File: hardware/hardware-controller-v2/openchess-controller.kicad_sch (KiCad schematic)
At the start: 30 parts, among them J1 Conn_02x13, J3 J_PANEL XH-10, M1 Lipo Rider Plus, U2 ESP32-DevKitC, U3 74AHCT125, U6 TBD62783A

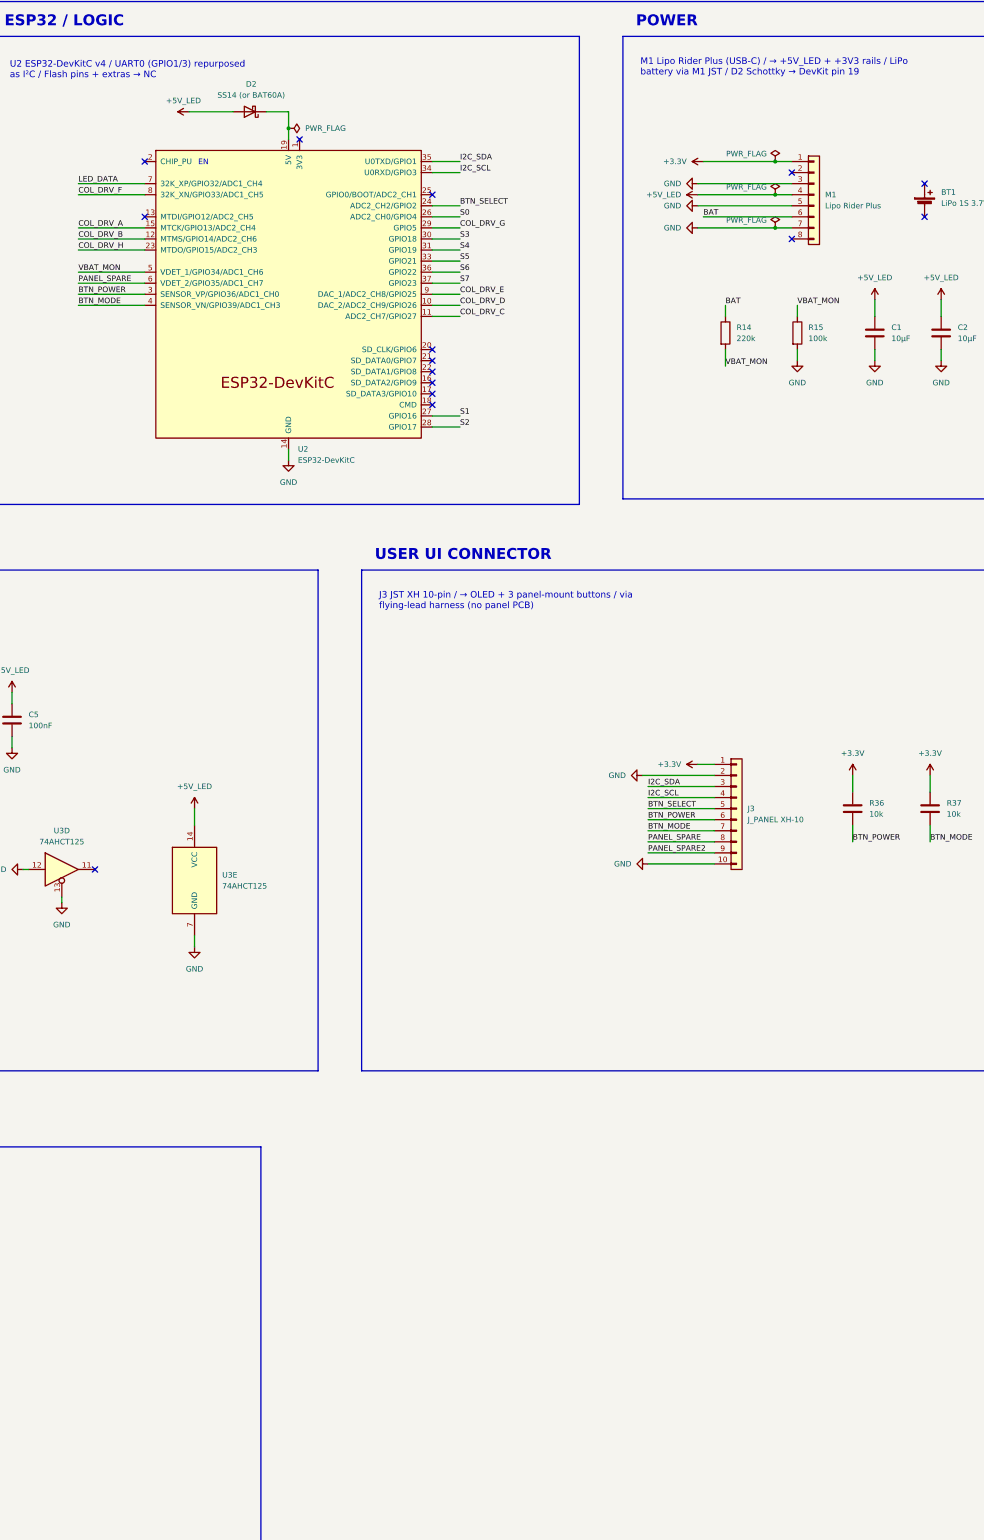
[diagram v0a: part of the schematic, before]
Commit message: feat(hw): v2 sch — WROOM-32E core hand-wired (power, EN/BOOT circuit)
Co-Authored-By: Claude Fable 5 <noreply@anthropic.com>
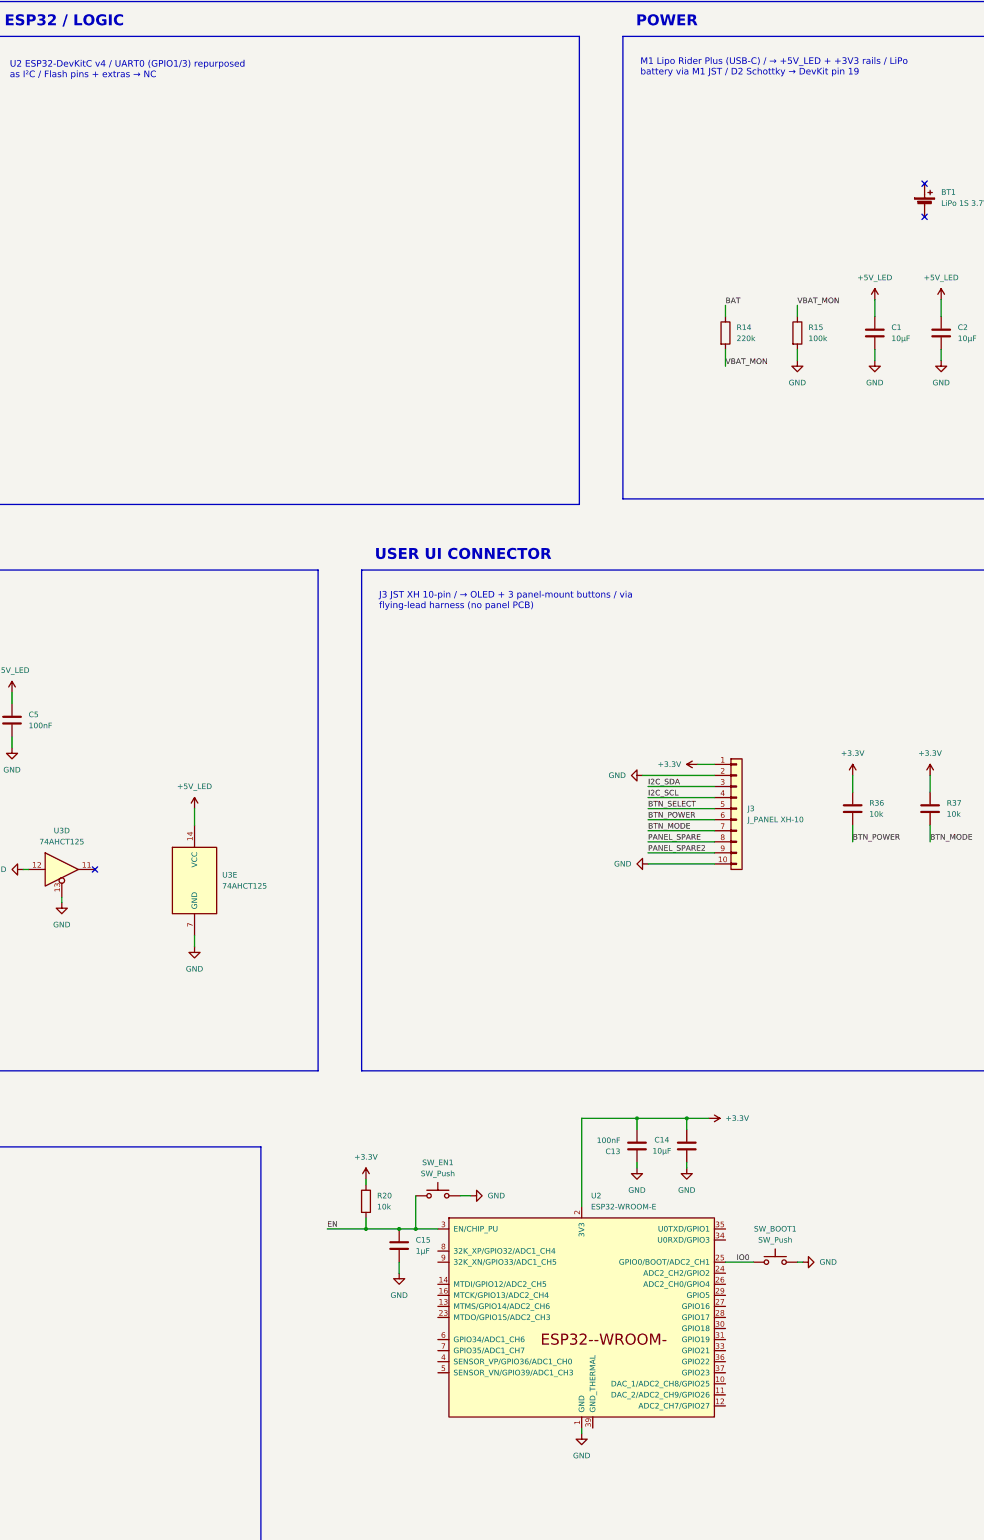
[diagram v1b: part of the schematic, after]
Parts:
- removed D2: SS14 (or BAT60A), Diode_SMD:D_SMA, symbol Device:D_Schottky
- removed M1: Lipo Rider Plus, Connector_PinSocket_2.54mm:PinSocket_1x08_P2.54mm_Vertical, symbol Connector_Generic:Conn_01x08
- removed U2: ESP32-DevKitC, Espressif:ESP32-DevKitC, symbol Espressif_Official:ESP32-DevKitC
- added C13: 100nF, symbol Device:C
- added C14: 10µF, symbol Device:C
- added C15: 1µF, symbol Device:C
- added R20: 10k, symbol Device:R
- added SW_BOOT1, SW_EN1: SW_Push, symbol Switch:SW_Push
- added U2: ESP32-WROOM-E, PCM_Espressif:ESP32-WROOM-32E, symbol Espressif_Official:ESP32-WROOM-E
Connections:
- net +3.3V: now also C13.1, C14.2, R20.1, U2.2 (3V3)
- net GND: now also C13.2, C14.1, C15.2, SW_BOOT1.2, SW_EN1.2, U2.1 (GND), U2.15 (GND), U2.38 (GND)
- new net EN: C15.1, R20.2, SW_EN1.1, U2.3 (EN/CHIP_PU)
- new net IO0: SW_BOOT1.1, U2.25 (GPIO0/BOOT/ADC2_CH1)
- no-connect marks 17 -> 5
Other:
- note removed: "EN"

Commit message: feat(hw): v2 sch — all 26 GPIO signal labels on WROOM core (27/27 contract)
Co-Authored-By: Claude Fable 5 <noreply@anthropic.com>
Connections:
- net BTN_MODE: now also U2.5 (SENSOR_VN/GPIO39/ADC1_CH3)
- net BTN_POWER: now also U2.4 (SENSOR_VP/GPIO36/ADC1_CH0)
- net BTN_SELECT: now also U2.24 (ADC2_CH2/GPIO2)
- net COL_DRV_A: now also U2.16 (MTCK/GPIO13/ADC2_CH4)
- net COL_DRV_B: now also U2.13 (MTMS/GPIO14/ADC2_CH6)
- net COL_DRV_C: now also U2.12 (ADC2_CH7/GPIO27)
- net COL_DRV_D: now also U2.11 (DAC_2/ADC2_CH9/GPIO26)
- net COL_DRV_E: now also U2.10 (DAC_1/ADC2_CH8/GPIO25)
- net COL_DRV_F: now also U2.9 (32K_XN/GPIO33/ADC1_CH5)
- net COL_DRV_G: now also U2.26 (ADC2_CH0/GPIO4)
- net COL_DRV_H: now also U2.14 (MTDI/GPIO12/ADC2_CH5)
- net GND: now also U2.39 (GND_THERMAL)
- net I2C_SCL: now also U2.36 (GPIO22)
- net I2C_SDA: now also U2.33 (GPIO21)
- net LED_DATA: now also U2.8 (32K_XP/GPIO32/ADC1_CH4)
- net S0: now also U2.27 (GPIO16)
- net S1: now also U2.28 (GPIO17)
- net S2: now also U2.30 (GPIO18)
- net S3: now also U2.31 (GPIO19)
- net S4: now also U2.37 (GPIO23)
- net S5: now also U2.29 (GPIO5)
- net S6: now also U2.23 (MTDO/GPIO15/ADC2_CH3)
- net S7: now also U2.7 (GPIO35/ADC1_CH7)
- net VBAT_MON: now also U2.6 (GPIO34/ADC1_CH6)
- net U0RXD: now reaches U2.34 (U0RXD/GPIO3)
- net U0TXD: now reaches U2.35 (U0TXD/GPIO1)
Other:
- note added: "OpenChess — Controller Board V2"
- note removed: "OpenChess — Controller Board"
- moved on the sheet: C15, R20, SW_BOOT1

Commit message: feat(hw): v2 sch — USB-C, CH340C, auto-program, ESD hand-wired (45/45 contract)
Co-Authored-By: Claude Fable 5 <noreply@anthropic.com>
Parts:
- added C16, C19: 100nF, symbol Device:C
- added J4: TYPE-C-31-M-12, symbol Connector:USB_C_Receptacle_USB2.0_16P
- added Q1, Q2: S8050 J3Y, Package_TO_SOT_SMD:SOT-23, symbol Transistor_BJT:SS8050
- added R21, R22: 5.1k, symbol Device:R
- added R23, R24: 10k, symbol Device:R
- added U7: CH340C, Package_SO:SOIC-16_3.9x9.9mm_P1.27mm, symbol Interface_USB:CH340C
- added U8: USBLC6-2SC6, Package_TO_SOT_SMD:SOT-23-6, symbol Power_Protection:USBLC6-2SC6
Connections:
- net EN: now also Q1.3 (C)
- net GND: now also C16.2, C19.2, J4.A1 (GND), J4.A12 (GND), J4.B1 (GND), J4.B12 (GND), J4.SH (SHIELD), R21.2, R22.2, U7.1 (GND), U8.2 (GND)
- net IO0: now also Q2.3 (C)
- net U0RXD: now also U7.2 (TXD)
- net U0TXD: now also U7.3 (RXD)
- new net: J4.A5 (CC1), R21.1
- new net: Q2.1 (B), R24.2
- new net: C19.1, U7.4 (V3)
- new net: J4.B5 (CC2), R22.1
- new net: Q1.1 (B), R23.2
- new net DTR: Q2.2 (E), R23.1, U7.13 (~{DTR})
- new net RTS: Q1.2 (E), R24.1, U7.14 (~{RTS})
- new net USB_DM: J4.A7 (D-), J4.B7 (D-), U7.6 (UD-), U8.3 (I/O2), U8.4 (I/O2)
- new net USB_DP: J4.A6 (D+), J4.B6 (D+), U7.5 (UD+), U8.1 (I/O1), U8.6 (I/O1)
- new net VBUS: C16.1, J4.A4 (VBUS), J4.A9 (VBUS), J4.B4 (VBUS), J4.B9 (VBUS), U7.16 (VCC), U8.5 (VBUS)
- no-connect marks 5 -> 12
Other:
- moved on the sheet: C13, C14, C15, R20, SW_BOOT1, SW_EN1, U2

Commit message: feat(hw): v2 sch — power chain hand-wired (80/80); checker refs adjudicated to as-built
R28/R29 and C17/C18 reference names landed swapped vs the guide; values sit on
the correct nets (1.1k=ILIM, 910R=ISET, 10uF on both LDO rails). As-built names
accepted; checker updated to match.

Co-Authored-By: Claude Fable 5 <noreply@anthropic.com>
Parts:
- removed BT1: LiPo 1S 3.7V (protected), symbol Device:Battery_Cell
- added C17, C18, C20, C21, C22: 10µF, symbol Device:C
- added C23: 100µF, symbol Device:C
- added C24, C25: 22µF, symbol Device:C
- added D4, D5: D, symbol Device:D
- added J5: B2B-XH-A, symbol Connector_Generic:Conn_01x02
- added L1: 1µH, symbol Device:L
- added R25, R27: 1k, symbol Device:R
- added R26: 100k, symbol Device:R
- added R28: 1.1K, symbol Device:R
- added R29: 910Ω, symbol Device:R
- added R30, R31, R32: 10k, symbol Device:R
- added SW1: MSK12C02, symbol Switch:SW_SPDT
- added U10: TPS61022RWUR, Package_DFN_QFN:Texas_RWU0007A_VQFN-7_2x2mm_P0.5mm, symbol Converter_DCDC:TPS61022
- added U11: AMS1117-3.3, Package_TO_SOT_SMD:SOT-223-3_TabPin2, symbol Regulator_Linear:AMS1117-3.3
- added U9: BQ24074RGTR, Package_DFN_QFN:VQFN-16-1EP_3x3mm_P0.5mm_EP1.6x1.6mm, symbol Battery_Management:BQ24074RGT
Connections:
- net +3.3V: now also C17.1, R27.1, U11.2 (VO), U9.5 (EN2)
- net +5V_LED: now also C18.1, C23.1, C24.1, C25.1, L1.2, R31.1, U10.3 (VOUT), U11.3 (VI)
- net GND: now also C17.2, C18.2, C20.1, C21.1, C22.1, C23.2, C24.2, C25.2, D5.1 (K), J5.2 (Pin_2), R26.2, R28.1, R29.1, R30.2, R32.2, U10.1 (GND), U10.6 (MODE), U11.1 (GND), U9.14 (TMR), U9.17 (VSS), U9.4 (~{CE}), U9.6 (EN1), U9.8 (VSS)
- net VBUS: now also C20.2, U9.13 (IN)
- net BAT renamed VBAT
- net VBAT: now also J5.1 (Pin_1), U9.2 (BAT), U9.3 (BAT)
- new net: L1.1, U10.2 (SW)
- new net: R31.2, R32.1, U10.4 (FB)
- new net: R26.1, SW1.1 (A), U10.5 (EN)
- new net: D5.2 (A), R27.2
- new net: R30.1, U9.1 (TS)
- new net: R28.2, U9.12 (ILIM)
- new net: R29.2, U9.16 (ISET)
- new net: D4.1 (K), U9.9 (~{CHG})
- new net: D4.2 (A), R25.1
- new net VSYS: C21.2, C22.2, R25.2, SW1.2 (B), U10.7 (VIN), U9.10 (OUT), U9.11 (OUT)
- no-connect marks 12 -> 13
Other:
- note added: "M1 Lipo Rider Plus (USB-C) / → +5V_LED + +3V3 rails / LiPo battery via M1 JST → DevKit pin 19"
- note removed: "M1 Lipo Rider Plus (USB-C) / → +5V_LED + +3V3 rails / LiPo battery via M1 JST / D2 Schottky → DevKit pin 19"
- moved on the sheet: C1, C11, C12, C13, C14, C15, C16, C19, C2, C5, FID1, FID2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

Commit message: fix(hw): v2 sch — FB divider values 750k/100k; checker now asserts component values
R31/R32 were both 10k (boost would regulate to 1.2V, not 5V) — caught by Paolo
visually; checker gap closed with value assertions for all power components.

Co-Authored-By: Claude Fable 5 <noreply@anthropic.com>
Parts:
- R31: value 10k -> 750k
- R32: value 10k -> 100k
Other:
- note removed: "M1 Lipo Rider Plus (USB-C) / → +5V_LED + +3V3 rails / LiPo battery via M1 JST → DevKit pin 19"
- note removed: "POWER"
- moved on the sheet: C1, C12, C16, C19, C2, FID1, FID2, FID3, FID4, J3, J4, Q1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

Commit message: feat(hw): v2 sch — panel split J6 OLED + J7/J8/J9 per-button XH-2; nets renamed BTN_UP/DOWN/OK
Button semantics follow firmware reality (ui_oled.cpp: UP/DOWN/OK; OK doubles
as deep-sleep wake). No dedicated power button; SW1 slide is power.

Co-Authored-By: Claude Fable 5 <noreply@anthropic.com>
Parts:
- removed J3: J_PANEL XH-10, Connector_PinHeader_2.54mm:PinHeader_1x10_P2.54mm_Vertical, symbol Connector_Generic:Conn_01x10
- added J6: J_OLED XH-4, symbol Connector_Generic:Conn_01x04
- added J7: J_BTN_UP XH-2, symbol Connector_Generic:Conn_01x02
- added J8: J_BTN_DOWN XH-2, symbol Connector_Generic:Conn_01x02
- added J9: J_BTN_OK XH-2, symbol Connector_Generic:Conn_01x02
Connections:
- net +3.3V: now also J6.2 (Pin_2)
- net GND: now also J6.1 (Pin_1), J7.2 (Pin_2), J8.2 (Pin_2), J9.2 (Pin_2)
- net I2C_SCL: now also J6.3 (Pin_3)
- net I2C_SDA: now also J6.4 (Pin_4)
- net BTN_MODE renamed BTN_DOWN
- net BTN_DOWN: now also J8.1 (Pin_1)
- net BTN_POWER renamed BTN_UP
- net BTN_UP: now also J7.1 (Pin_1)
- net BTN_SELECT renamed BTN_OK
- net BTN_OK: now also J9.1 (Pin_1)

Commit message: feat(hw): v2 sch — ERC zero errors (PWR_FLAG on GND); schematic wiring complete
Co-Authored-By: Claude Fable 5 <noreply@anthropic.com>
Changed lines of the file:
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@@
 	)
 	(junction
-		(at 354.33 273.0032)
+		(at 469.9 289.56)
 		(diameter 0)
 		(color 0 0 0 0)
 	)
 	(junction
-		(at 469.9 289.56)
+		(at 354.33 273.05)
 		(diameter 0)
 		(color 0 0 0 0)
@@
 	)
 	(junction
+		(at 360.68 147.32)
+		(diameter 0)
+		(color 0 0 0 0)
+	)
+	(junction
 		(at 457.2 303.53)
 		(diameter 0)
@@
 	(wire
 		(pts
-			(xy 354.33 270.51) (xy 354.33 273.0032)
-		)
-		(stroke
-			(width 0)
-			(type default)
-		)
-	)
-	(wire
-		(pts
 			(xy 443.23 337.82) (xy 443.23 341.63)
 		)
@@
 	(wire
 		(pts
+			(xy 354.33 270.51) (xy 354.33 273.05)
+		)
+		(stroke
+			(width 0)
+			(type default)
+		)
+	)
+	(wire
+		(pts
 			(xy 313.69 224.79) (xy 314.96 224.79)
 		)
@@
 	(wire
 		(pts
-			(xy 353.06 273.05) (xy 354.33 273.0032)
-		)
-		(stroke
-			(width 0)
-			(type default)
-		)
-	)
-	(wire
-		(pts
 			(xy 396.24 99.06) (xy 393.7 99.06)
 		)
@@
 	(wire
 		(pts
-			(xy 360.68 146.05) (xy 360.68 144.78)
+			(xy 360.68 148.59) (xy 360.68 147.32)
 		)
 		(stroke
@@
 	(wire
 		(pts
+			(xy 353.06 273.05) (xy 354.33 273.05)
+		)
+		(stroke
+			(width 0)
+			(type default)
+		)
+	)
+	(wire
+		(pts
 			(xy 72.39 217.17) (xy 78.74 217.17)
 		)
@@
 	(wire
 		(pts
-			(xy 354.33 273.0032) (xy 354.33 275.59)
-		)
-		(stroke
-			(width 0)
-			(type default)
-		)
-	)
-	(wire
-		(pts
 			(xy 165.1 300.99) (xy 165.1 302.26)
 		)
@@
 	(wire
 		(pts
-			(xy 363.22 152.4) (xy 363.22 144.78)
+			(xy 363.22 156.21) (xy 363.22 144.78)
 		)
 		(stroke
@@
 	(wire
 		(pts
+			(xy 354.33 273.05) (xy 354.33 275.59)
+		)
+		(stroke
+			(width 0)
+			(type default)
+		)
+	)
+	(wire
+		(pts
 			(xy 259.08 298.45) (xy 260.35 298.45)
 		)
@@
 	(wire
 		(pts
+			(xy 360.68 147.32) (xy 360.68 144.78)
+		)
+		(stroke
+			(width 0)
+			(type default)
+		)
+	)
+	(wire
+		(pts
 			(xy 387.35 280.67) (xy 383.54 280.67)
 		)
@@
 	)
 	(symbol
+		(lib_id "power:PWR_FLAG")
+		(at 360.68 147.32 90)
+		(unit 1)
+		(body_style 1)
+		(exclude_from_sim no)
+		(in_bom yes)
+		(on_board yes)
+		(in_pos_files yes)
+		(dnp no)
+		(fields_autoplaced yes)
+		(property "Reference" "#FLG04"
+			(at 358.775 147.32 0)
+			(hide yes)
+			(show_name no)
+			(do_not_autoplace no)
+			(effects
+				(font
+					(size 1.27 1.27)
+				)
+			)
+		)
+		(property "Value" "PWR_FLAG"
+			(at 356.87 147.3199 90)
+			(show_name no)
+			(do_not_autoplace no)
+			(effects
+				(font
+					(size 1.27 1.27)
+				)
+				(justify left)
+			)
+		)
+		(property "Footprint" ""
+			(at 360.68 147.32 0)
+			(hide yes)
+			(show_name no)
+			(do_not_autoplace no)
+			(effects
+				(font
+					(size 1.27 1.27)
+				)
+			)
+		)
+		(property "Datasheet" ""
+			(at 360.68 147.32 0)
+			(hide yes)
+			(show_name no)
+			(do_not_autoplace no)
+			(effects
+				(font
+					(size 1.27 1.27)
+				)
+			)
+		)
+		(property "Description" "Special symbol for telling ERC where power comes from"
+			(at 360.68 147.32 0)
+			(hide yes)
+			(show_name no)
+			(do_not_autoplace no)
+			(effects
+				(font
+					(size 1.27 1.27)
+				)
+			)
+		)
+		(pin "1"
+		)
+		(instances
+			(project "openchess-controller"
+				(path "/ab0a4d00-0000-4000-8000-000000000001"
+					(reference "#FLG04")
+					(unit 1)
+				)
+			)
+		)
+	)
+	(symbol
 		(lib_id "Device:C")
 		(at 435.61 308.61 270)
@@
 	(symbol
 		(lib_id "power:GND")
-		(at 360.68 146.05 0)
+		(at 360.68 148.59 0)
 		(unit 1)
 		(body_style 1)
@@
 		(fields_autoplaced yes)
 		(property "Reference" "#PWR03"
-			(at 360.68 152.4 0)
+			(at 360.68 154.94 0)
 			(hide yes)
 			(show_name no)
@@
 		)
 		(property "Value" "GND"
-			(at 360.68 151.13 0)
+			(at 360.68 153.67 0)
 			(show_name no)
 			(do_not_autoplace no)
@@
 		)
 		(property "Footprint" ""
-			(at 360.68 146.05 0)
+			(at 360.68 148.59 0)
 			(hide yes)
 			(show_name no)
@@
 		)
 		(property "Datasheet" ""
-			(at 360.68 146.05 0)
+			(at 360.68 148.59 0)
 			(hide yes)
 			(show_name no)
@@
 		)
 		(property "Description" "Power symbol creates a global label with name \"GND\" , ground"
-			(at 360.68 146.05 0)
+			(at 360.68 148.59 0)
 			(hide yes)
 			(show_name no)
@@
 	(symbol
 		(lib_id "power:GND")
-		(at 363.22 152.4 0)
+		(at 363.22 156.21 0)
 		(unit 1)
 		(body_style 1)
@@
 		(fields_autoplaced yes)
 		(property "Reference" "#PWR037"
-			(at 363.22 158.75 0)
+			(at 363.22 162.56 0)
 			(hide yes)
 			(show_name no)
@@
 		)
 		(property "Value" "GND"
-			(at 363.22 157.48 0)
+			(at 363.22 161.29 0)
 			(show_name no)
 			(do_not_autoplace no)
@@
 		)
 		(property "Footprint" ""
-			(at 363.22 152.4 0)
+			(at 363.22 156.21 0)
 			(hide yes)
 			(show_name no)
@@
 		)
 		(property "Datasheet" ""
-			(at 363.22 152.4 0)
+			(at 363.22 156.21 0)
 			(hide yes)
 			(show_name no)
@@
 		)
 		(property "Description" "Power symbol creates a global label with name \"GND\" , ground"
-			(at 363.22 152.4 0)
+			(at 363.22 156.21 0)
 			(hide yes)
 			(show_name no)

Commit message: feat(hw): v2 footprints and LCSC fields; docs updated to as-built panel/buttons
- Assign footprints to all v2 symbols: ESP32-WROOM-32E (RF_Module), CH340C
  (SOIC-16), USB-C (HRO TYPE-C-31-M-12), USBLC6-2SC6 (SOT-23-6), BQ24074
  (VQFN-16-1EP 3x3mm ThermalVias), TPS61022 (Texas RWU VQFN-7 2x2mm),
  AMS1117-3.3 (SOT-223-3_TabPin2), TBD62783A (SOP-18), Q1/Q2 SS8050 (SOT-23),
  L1 APH0420T (L_APV_APH0420), D4/D5 (LED_0603), SW1 MSK12C02, SW_EN1/BOOT1
  TS-1187A, J5/J7/J8/J9 (JST XH B2B-XH-A), J6 (JST XH B4B-XH-A), new 0603 R
  and C values throughout
- Fix U2 footprint: replace PCM_Espressif:ESP32-WROOM-32E with standard
  RF_Module:ESP32-WROOM-32E (removes ERC footprint library warning)
- Add LCSC fields to all JLC-assembled parts; match by VALUE+ROLE per as-built
  deviation note (R28=C22764, R29=no C# yet, etc.)
- docs/gpio-map.md: BTN_POWER/MODE -> BTN_DOWN/UP in v2 section only
- docs/inter-board-connector.md: replace J_BTN XH-5 with J7/J8/J9 XH-2 tables
- SOURCING.md: drop B5B-XH-A 5-pin; count now 4x B2B-XH-A + 1x B4B-XH-A;
  add R21/R22 5.1k CC pulldown row (assign at order time)
- ERC: 0 violations; check_task6: 45/45; check_task7: 89/89

Co-Authored-By: Claude Fable 5 <noreply@anthropic.com>
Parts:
- C13, C15, C16, C19: footprint (none) -> Capacitor_SMD:C_0603_1608Metric
- C14, C17, C18, C20, C21, C22, C24, C25: footprint (none) -> Capacitor_SMD:C_0805_2012Metric
- C23: footprint (none) -> Capacitor_SMD:CP_Elec_6.3x5.4
- D4: footprint (none) -> LED_SMD:LED_0603_1608Metric; LCSC (none) -> C2286
- D5: footprint (none) -> LED_SMD:LED_0603_1608Metric; LCSC (none) -> C12624
- J4: footprint (none) -> Connector_USB:USB_C_Receptacle_HRO_TYPE-C-31-M-12; LCSC (none) -> C165948
- J5, J7, J8, J9: footprint (none) -> Connector_JST:JST_XH_B2B-XH-A_1x02_P2.50mm_Vertical
- J6: footprint (none) -> Connector_JST:JST_XH_B4B-XH-A_1x04_P2.50mm_Vertical
- L1: footprint (none) -> Inductor_SMD:L_APV_APH0420; LCSC (none) -> C5349664
- Q1, Q2: LCSC (none) -> C42441446
- R1, R2, R3, R36, R37, R4, R5, R6, R7, R8: LCSC (none) -> C25804
- R15: LCSC (none) -> C25803
- R20, R23, R24, R30: footprint (none) -> Resistor_SMD:R_0603_1608Metric; LCSC (none) -> C25804
- R21, R22, R29: footprint (none) -> Resistor_SMD:R_0603_1608Metric
- R25, R27: footprint (none) -> Resistor_SMD:R_0603_1608Metric; LCSC (none) -> C21190
- R26, R32: footprint (none) -> Resistor_SMD:R_0603_1608Metric; LCSC (none) -> C25803
- R28: footprint (none) -> Resistor_SMD:R_0603_1608Metric; LCSC (none) -> C22764
- R31: footprint (none) -> Resistor_SMD:R_0603_1608Metric; LCSC (none) -> C23240
- SW1: footprint (none) -> Button_Switch_SMD:SW_SPDT_Shouhan_MSK12C02; LCSC (none) -> C431540
- SW_BOOT1, SW_EN1: footprint (none) -> Button_Switch_SMD:SW_Push_1P1T_XKB_TS-1187A; LCSC (none) -> C318884
- U10: LCSC (none) -> C915088
- U11: LCSC (none) -> C6186
- U2: footprint PCM_Espressif:ESP32-WROOM-32E -> RF_Module:ESP32-WROOM-32E; LCSC (none) -> C701341
- U3: LCSC (none) -> C2139
- U6: footprint Package_DIP:DIP-18_W7.62mm -> Package_SO:SOP-18_7.495x11.515mm_P1.27mm; LCSC (none) -> C97745
- U7: LCSC (none) -> C84681
- U8: LCSC (none) -> C7519
- U9: footprint Package_DFN_QFN:VQFN-16-1EP_3x3mm_P0.5mm_EP1.6x1.6mm -> Package_DFN_QFN:VQFN-16-1EP_3x3mm_P0.5mm_EP1.6x1.6mm_ThermalVias; LCSC (none) -> C54313
